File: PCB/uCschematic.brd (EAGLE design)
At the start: 100 x 80 mm, 62 parts, among them IC1 PIC24FJXXGA002/SO, IC10 ULN2003D1013TR, IC11 ULN2003D1013TR, IC12 ULN2003D1013TR, IC2 317EMP, IC3 MC74HC175ADG, IC4 MC74HC175ADG, IC5 MC74HC175ADG, IC6 MC74HC175ADG, IC7 MC74HC175ADG, IC8 MC74HC175ADG, IC9 ULN2003D1013TR, U1 74HC237D-Q100J

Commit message: SPI, I2C, 4 granicna prekidaca, DONE
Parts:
- added CAT_ANGLE, CAT_ROTATION, CS, GP_LASER1, GP_LASER2, MISO, SCLK/SCL, SDA/MOSI: PIN1-2, con-faston:62221
- added R10, R5, R6, R7, R8, R9: 10k, eagle-ltspice:R0805
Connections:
- removed net RST: IC1.17, IC3.1, IC4.1, IC5.1, IC6.1, IC7.1, IC8.1
- new net N$29: GP_LASER2.1, IC1.3, R6.2
- new net N$37: CAT_ROTATION.1, IC1.2, R7.2
- new net N$38: CAT_ANGLE.1, IC1.16, R8.1
- new net N$39: CS.1, IC1.23
- new net N$40: IC1.24, MISO.1
- new net N$41: IC1.25, R10.2, SDA/MOSI.1
- new net N$42: IC1.26, R9.2, SCLK/SCL.1
- net 3.3V: now also IC3.1, IC4.1, IC5.1, IC6.1, IC7.1, IC8.1, R10.1, R9.1
- net GND: now also R5.1, R6.1, R7.1, R8.2, U1.6
- net N$17: now also GP_LASER1.1, IC1.12, R5.2; no longer IC1.16, U1.6
- net N$25: now also IC1.18; no longer IC1.26
- net N$26: now also IC1.17; no longer IC1.25

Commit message: Uradjene izmjene PIN19 spojen na GND Kapacitivnost kondenzatora kod kristala kvarca je sada 47pF Dodana je masa za svaki od GP Dodana je masa za SPI i I2C Dodane su mase za koracne motore LATCH i ENABLE sada su na dobrim logickim nivoima
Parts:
- added GND_CAT_ANGLE, GND_CAT_ROTATION, GND_GP_LASER1, GND_GP_LASER2, GND_SM1, GND_SM2, GND_SM3, GND_SM4, GND_SM5, GND_SM6, GND_SPI/I2C: PIN1-2, con-faston:62221
- C6, C8: value 100nF -> 47pF
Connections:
- net 3.3V: now also U1.6
- net GND: now also GND_CAT_ANGLE.1, GND_CAT_ROTATION.1, GND_GP_LASER1.1, GND_GP_LASER2.1, GND_SM1.1, GND_SM2.1, GND_SM3.1, GND_SM4.1, GND_SM5.1, GND_SM6.1, GND_SPI/I2C.1, IC1.19; no longer U1.6

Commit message: Uradjena sema za USB/UART converter
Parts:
- removed RX, TX: PIN1-2, con-faston:62221
- added C10, C11: 47pF, eagle-ltspice:C0805
- added C9: 0.1u, eagle-ltspice:C0805
- added IC13: FT230XS-U, FT230XS-U:SOP64P599X175-16N
- added J1: USB3075-30-A, USB3075-30-A:USB307530A
- added R11, R12: 27, rcl:R0805
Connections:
- new net N$45: C10.2, J1.2, R11.2
- new net N$53: C9.2, IC13.10, IC13.11, IC13.3
- new net N$54: C11.2, J1.3, R12.2
- new net N$55: IC13.9, R11.1
- new net N$56: IC13.8, R12.1
- net 3.3V: now also IC13.12
- net GND: now also C10.1, C11.1, C9.1, IC13.13, IC13.5, J1.5, J1.MH1, J1.MH2, J1.MP1, J1.MP2, J1.MP3, J1.MP4
- net N$25: now also IC13.4; no longer RX.1
- net N$26: now also IC13.1; no longer TX.1

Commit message: -Dodani bajpas kondenzatori.
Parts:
- added C12, C13, C14, C15, C16, C17, C18, C19, C20, C21, C22, C23, C24, C25, C26: 0.1u, capacitor-wima:C2.5-3
- C4: value 0.1u -> 1u
- R3: value 470 -> 240
- R4: value 770,8 -> 390
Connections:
- new net N$28: C24.2
- new net N$58: C25.2
- new net N$59: C23.2
- new net N$60: C26.2
- new net N$61: C22.2
- new net N$69: C21.2
- new net N$70: C19.2
- new net N$71: C20.2
- new net N$72: C18.2
- new net N$77: C17.2
- new net N$85: C15.2
- net 3.3V: now also C12.1, C13.1, C14.1, C15.1, C16.1, C17.1, C18.1, C19.1, C20.1, C21.1, C22.1, C23.1, C24.1, C25.1, C26.1
- net GND: now also C12.2, C13.2, C14.2, C16.2

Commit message: -Unesene potrebne izmjene
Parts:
- removed C13, C16, C18, C20, C22, C24, C26: 0.1u, capacitor-wima:C2.5-3
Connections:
- removed net N$28: C24.2
- removed net N$60: C26.2
- removed net N$61: C22.2
- removed net N$71: C20.2
- removed net N$72: C18.2
- net 3.3V: no longer C13.1, C16.1, C18.1, C20.1, C22.1, C24.1, C26.1
- net GND: no longer C13.2, C16.2

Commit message: Osiguravanje dodatnog GP u slucaju da bude potreban.
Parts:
- removed C21, C23, C25: 0.1u, capacitor-wima:C2.5-3
- added C13, C16, C18: 0.1u, eagle-ltspice:C0805
- added GND_GP_1, GP, GP_1, PGEC/GP, PGEC_PROG: PIN1-2, con-faston:62221
- C12, C14, C15, C17, C19: device capacitor-wima:C2.5-3 -> eagle-ltspice:C0805
- moved C19 96.5 mm to (-588.0, -229.9)
- moved C17 96.5 mm to (-588.0, -217.2)
- moved C12 92.7 mm to (-588.0, -179.1)
- moved C14 91.4 mm to (-588.0, -191.8)
- moved C15 90.2 mm to (-588.0, -198.1)
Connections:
- new net GP_1: GP.1, GP_1.1
- new net N$28: PGEC.1, PGEC_PROG.1
- net 3.3V: now also C12.2, C13.2, C14.2, C15.2, C16.2, C17.2, C18.2, C19.2; no longer C12.1, C14.1, C15.1, C17.1, C19.1, C21.1, C23.1, C25.1
- net GND: now also C12.1, C14.1, GND_GP_1.1; no longer C12.2, C14.2
- net N$24: now also PGEC/GP.1; no longer PGEC.1
- net N$58: now also C19.1; no longer C25.2
- net N$59: now also C18.1; no longer C23.2
- net N$69: now also C17.1; no longer C21.2
- net N$70: now also C16.1; no longer C19.2
- net N$77: now also C13.1; no longer C17.2
- net N$85: now also C15.1; no longer C15.2

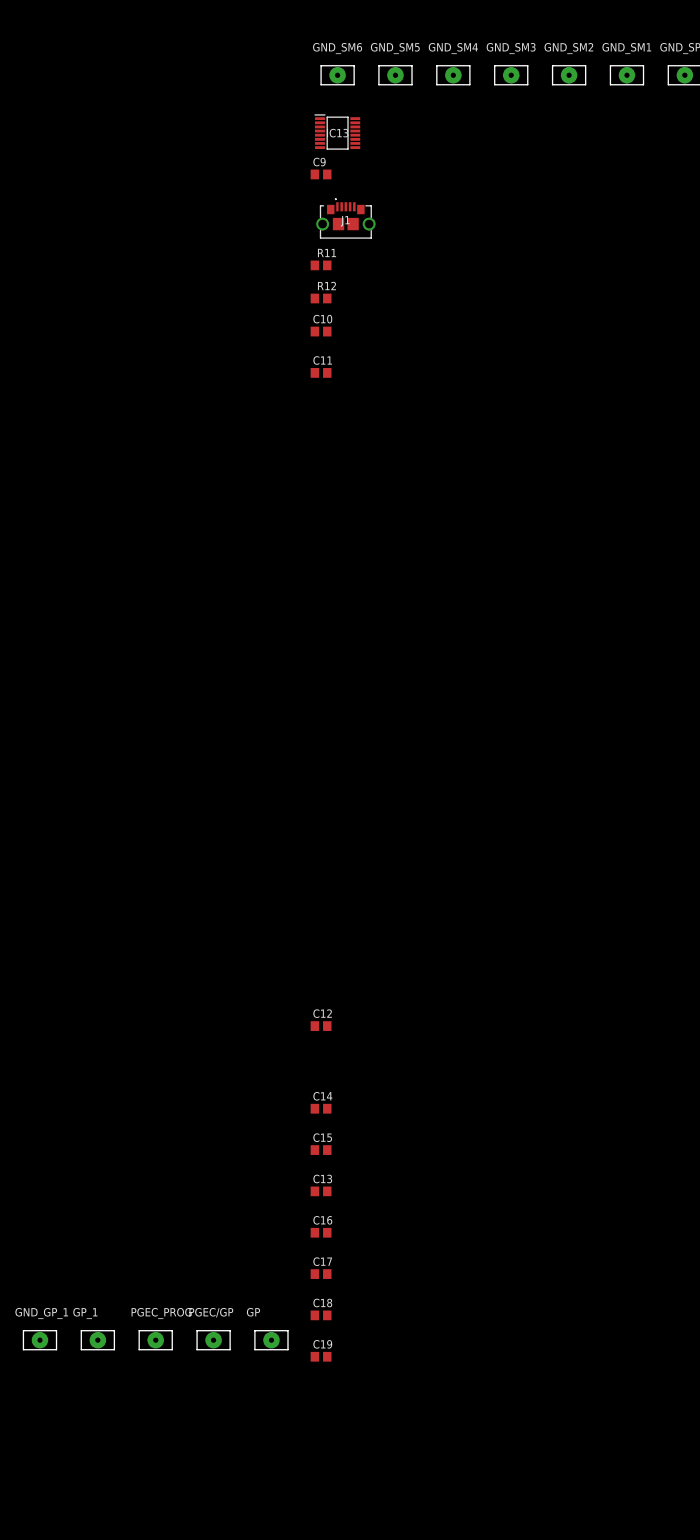
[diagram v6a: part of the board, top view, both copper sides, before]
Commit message: Uradjena simulacija u proteusu USB micro AB -> USB type A Izvrsena simulacija u proteusu. Sve radi kako treba Izvrsene sitne izmjene na semi
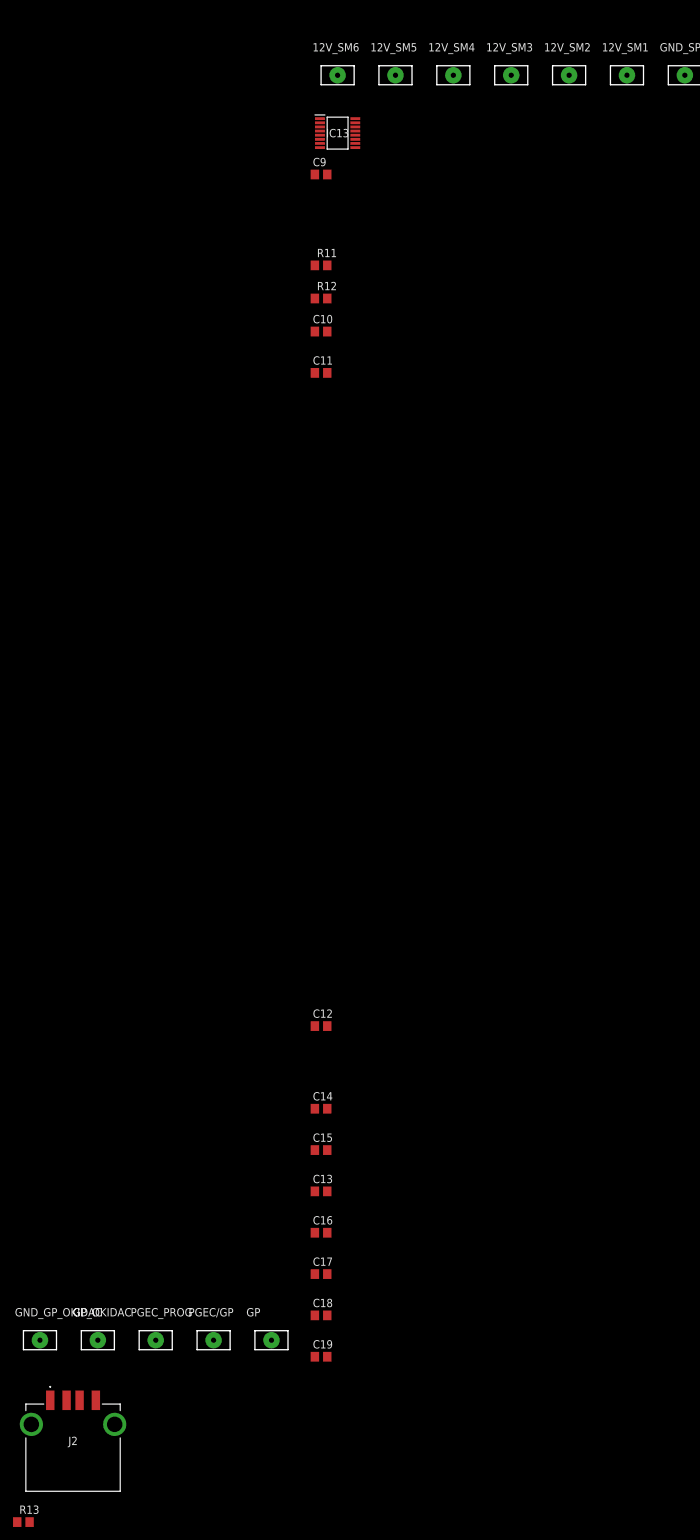
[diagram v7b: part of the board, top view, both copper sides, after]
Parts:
- removed J1: USB3075-30-A, USB3075-30-A:USB307530A
- added J2: USB1046-GF-0190-L-B-A, USB1046-GF-0190-L-B-A:USB1046GF0190LBA
- added R13: 10k, eagle-ltspice:R0805
- renumbered GND_GP_1 to GND_GP_OKIDAC, GND_SM1 to 12V_SM1, GND_SM2 to 12V_SM2, GND_SM3 to 12V_SM3, GND_SM4 to 12V_SM4, GND_SM5 to 12V_SM5, GND_SM6 to 12V_SM6, GP_1 to GP_OKIDAC
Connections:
- removed net GP_1: GP.1, GP_OKIDAC.1
- removed net VDD: C5.2, IC10.9, IC11.9, IC12.9, IC2.3, IC9.9, VDD.1
- new net 12V: 12V_SM1.1, 12V_SM2.1, 12V_SM3.1, 12V_SM4.1, 12V_SM5.1, 12V_SM6.1, C5.2, IC10.9, IC11.9, IC12.9, IC2.3, IC9.9, VDD.1
- new net GP_OKIDAC: GP.1, GP_OKIDAC.1, R13.2
- net 3.3V: now also R13.1, R5.1, R6.1, R7.1, R8.2
- net GND: now also J2.4, J2.MH1, J2.MH2; no longer 12V_SM1.1, 12V_SM2.1, 12V_SM3.1, 12V_SM4.1, 12V_SM5.1, 12V_SM6.1, J1.5, J1.MH1, J1.MH2, J1.MP1, J1.MP2, J1.MP3, J1.MP4, R5.1, R6.1, R7.1, R8.2
- net N$45: now also J2.2; no longer J1.2
- net N$54: now also J2.3; no longer J1.3
